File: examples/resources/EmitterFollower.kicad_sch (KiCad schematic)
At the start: 5 parts

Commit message: prob wont compile but the new circuit
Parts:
- added high_gate, low_gate: ~, Package_SO:TSOP-6_1.65x3.05mm_P0.95mm, symbol Analog_Switch:DG9421DV
- added high_res: 100k, symbol Device:R
- added res: 1k, symbol Device:R
- low_res: renamed from res; value 1k -> 100k
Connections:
- net control: now also res.1; no longer low_res.2
- net gnd: now also high_gate.4 (GND), low_gate.4 (GND)
- net out: now also low_res.2, high_res.2
- net at low_fet.2 (G), low_res.1: now also low_gate.5; no longer clamp1.2 (A), high_fet.2 (G)
- new net: clamp1.2 (A), high_gate.2, low_gate.2, res.2
- new net: high_fet.2 (G), high_gate.5, high_res.1
- new net high_gate: high_gate.6
- new net low_gate: low_gate.6
- new net pwr_gate_neg: high_gate.3 (V-), low_gate.3 (V-)
- new net pwr_gate_pos: high_gate.1 (V+), low_gate.1 (V+)
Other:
- moved on the sheet: low_res

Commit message: Update EmitterFollower.kicad_sch
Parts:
- removed high_gate, low_gate: ~, Package_SO:TSOP-6_1.65x3.05mm_P0.95mm, symbol Analog_Switch:DG9421DV
- added high_gate, low_gate: #AnalogMuxer(), symbol edg_importable:Mux2
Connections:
- net gnd: now also high_gate. (V-), low_gate. (V-)
- net pwr_gate_pos: now also high_gate. (V-), low_gate. (V-)
- net at clamp1.2 (A), res.2: now also high_gate.2, low_gate.2
- net at low_fet.2 (G), low_res.1: now also high_gate.C
- net at high_fet.2 (G), high_res.1: now also low_gate.C
- no-connect marks 0 -> 2
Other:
- moved on the sheet: high_fet, high_res, low_fet, low_res

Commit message: emitter follower builds
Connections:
- net at low_fet.2 (G), low_res.1: now also low_gate.C; no longer high_gate.C
- net at high_fet.2 (G), high_res.1: now also high_gate.C; no longer low_gate.C
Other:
- moved on the sheet: high_gate, low_gate
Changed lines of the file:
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@@
-	)
-	(junction
-		(at 93.98 107.95)
-		(diameter 0)
-		(color 0 0 0 0)
 	)
 	(junction
@@
 	(junction
 		(at 114.3 97.79)
+		(diameter 0)
+		(color 0 0 0 0)
+	)
+	(junction
+		(at 93.98 107.95)
 		(diameter 0)
 		(color 0 0 0 0)
@@
 		(lib_name "edg_importable:Mux2")
 		(lib_id "edg_importable:Mux2")
-		(at 88.9 107.95 0)
+		(at 88.9 82.55 0)
 		(mirror y)
 		(unit 1)
@@
 		(dnp no)
 		(property "Reference" "high_gate"
-			(at 88.9 115.57 0)
+			(at 88.9 90.17 0)
 			(effects
 				(font
@@
 		)
 		(property "Value" "#AnalogMuxer()"
-			(at 88.9 116.84 0)
+			(at 88.9 91.44 0)
 			(effects
 				(font
@@
 		)
 		(property "Footprint" ""
-			(at 88.9 107.95 0)
+			(at 88.9 82.55 0)
 			(effects
 				(font
@@
 		)
 		(property "Datasheet" "~"
-			(at 88.9 107.95 0)
+			(at 88.9 82.55 0)
 			(effects
 				(font
@@
 		)
 		(property "Description" ""
-			(at 88.9 107.95 0)
+			(at 88.9 82.55 0)
 			(effects
 				(font
@@
 		(dnp no)
 		(property "Reference" "low_res"
-			(at 102.87 111.76 90)
+			(at 102.87 106.934 90)
 			(effects
 				(font
@@
 		(lib_name "edg_importable:Mux2")
 		(lib_id "edg_importable:Mux2")
-		(at 88.9 82.55 0)
+		(at 88.9 107.95 0)
 		(mirror y)
 		(unit 1)
@@
 		(dnp no)
 		(property "Reference" "low_gate"
-			(at 88.9 90.17 0)
+			(at 88.9 115.57 0)
 			(effects
 				(font
@@
 		)
 		(property "Value" "#AnalogMuxer()"
-			(at 88.9 91.44 0)
+			(at 88.9 116.84 0)
 			(effects
 				(font
@@
 		)
 		(property "Footprint" ""
-			(at 88.9 82.55 0)
+			(at 88.9 107.95 0)
 			(effects
 				(font
@@
 		)
 		(property "Datasheet" "~"
-			(at 88.9 82.55 0)
+			(at 88.9 107.95 0)
 			(effects
 				(font
@@
 		)
 		(property "Description" ""
-			(at 88.9 82.55 0)
-			(effects
-				(font
+			(at 88.9 107.95 0)
+			(effects
+				(font

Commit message: to erc almost clean
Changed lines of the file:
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@@
 	)
 	(symbol
+		(lib_name "D_Zener_1")
 		(lib_id "Device:D_Zener")
 		(at 100.33 95.25 180)

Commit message: proper negative rails
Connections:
- net gnd: no longer high_gate. (V-), low_gate. (V-)
- new net pwr_gate_neg: high_gate. (V-), low_gate. (V-)
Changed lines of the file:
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@@
 		)
 	)
-	(global_label "gnd"
+	(global_label "pwr_gate_neg"
 		(shape input)
 		(at 87.63 113.03 180)
@@
 		)
 		(property "Intersheetrefs" "${INTERSHEET_REFS}"
-			(at 81.1978 113.03 0)
+			(at 71.945 113.03 0)
 			(effects
 				(font
@@
 		)
 	)
-	(global_label "gnd"
+	(global_label "pwr_gate_neg"
 		(shape input)
 		(at 87.63 87.63 180)
@@
 		)
 		(property "Intersheetrefs" "${INTERSHEET_REFS}"
-			(at 81.1978 87.63 0)
+			(at 71.945 87.63 0)
 			(effects
 				(font
@@
 	)
 	(symbol
-		(lib_name "edg_importable:Mux2")
 		(lib_id "edg_importable:Mux2")
 		(at 88.9 82.55 0)
@@
 	)
 	(symbol
-		(lib_name "edg_importable:Mux2")
 		(lib_id "edg_importable:Mux2")
 		(at 88.9 107.95 0)

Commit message: cap spam
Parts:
- added cap_in1, cap_in2, cap_in3: #DecouplingCapacitor(, symbol Device:C
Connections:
- net gnd: now also cap_in1.2, cap_in2.2, cap_in3.2
- net pwr: now also cap_in1.1, cap_in2.1, cap_in3.1
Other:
- note added: "These should be laid out as close to the FETs as possible"

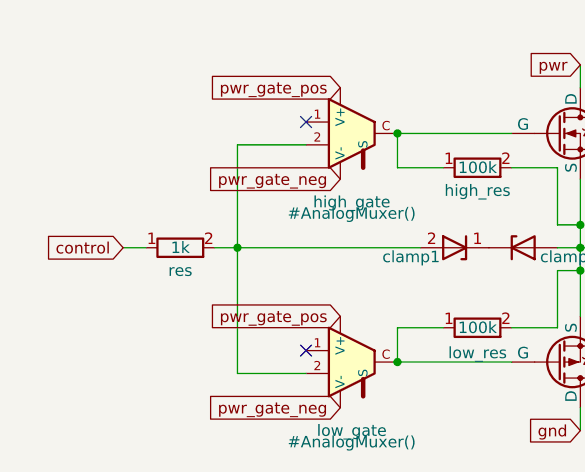
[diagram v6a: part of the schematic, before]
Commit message: model clamp pdis
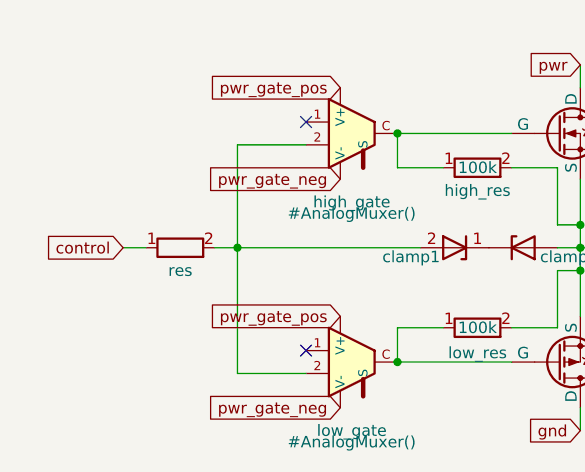
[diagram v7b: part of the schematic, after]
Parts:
- res: value 1k -> (none)
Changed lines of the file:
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@@
 			)
 		)
-		(property "Value" "1k"
+		(property "Value" ""
 			(at 69.85 95.25 90)
 			(effects

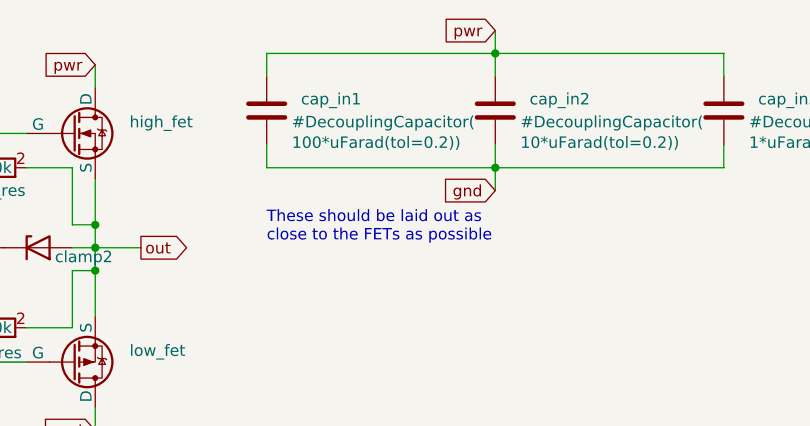
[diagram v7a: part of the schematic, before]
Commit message: fabrication optimization
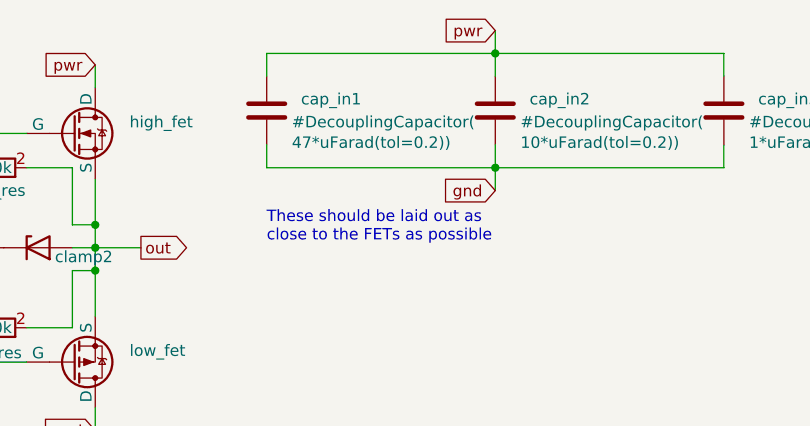
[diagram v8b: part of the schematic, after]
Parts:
- cap_in1: Value2 100*uFarad(tol=0.2)) -> 47*uFarad(tol=0.2))
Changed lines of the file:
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@@
 			)
 		)
-		(property "Value2" "100*uFarad(tol=0.2))"
+		(property "Value2" "47*uFarad(tol=0.2))"
 			(at 136.144 83.566 0)
 			(effects
